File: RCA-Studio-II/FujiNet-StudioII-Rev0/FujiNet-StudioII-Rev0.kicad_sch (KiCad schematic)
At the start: 0 parts

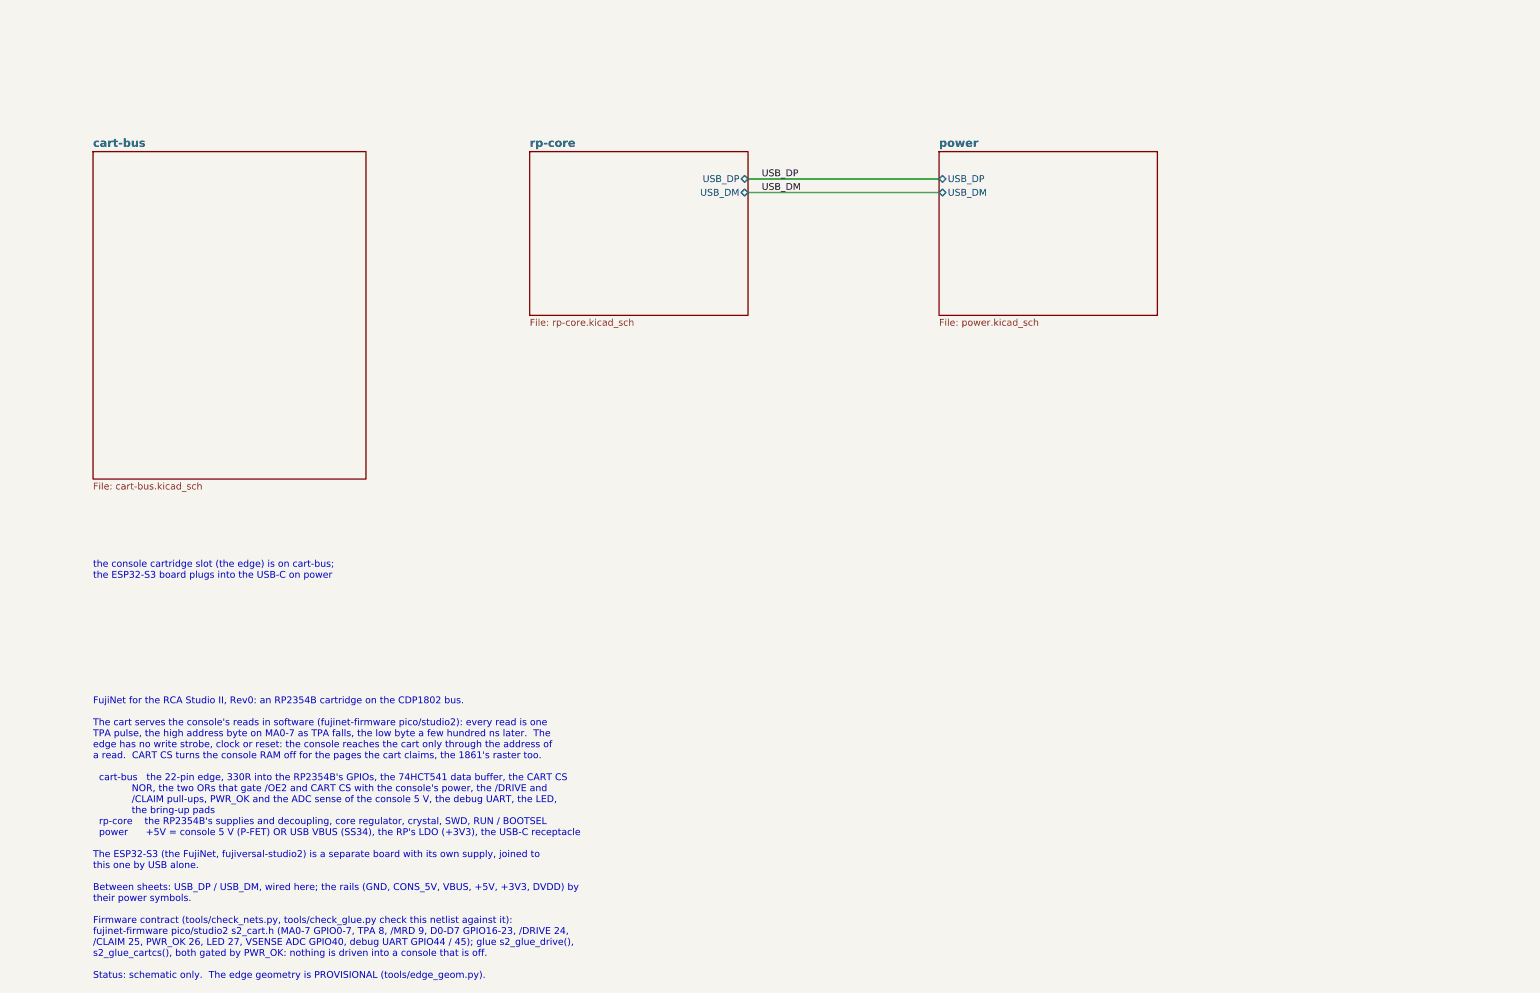
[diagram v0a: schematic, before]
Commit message: Studio II Rev0: ESP32-S3 on the cart, 4-layer board, JLCPCB package
The schematic is redone with the FujiNet's ESP32-S3 on the cartridge (it was
on a separate board), and the board is laid out, routed and audited for
JLCPCB assembly.

Schematic (5 sheets: cart-bus, rp-core, fujinet, usb, power):
- ESP32-S3-WROOM-1-N16R8 as the FujiNet and the RP2354B's USB host, with
  microSD, WS2812, EN RC and buttons (ported from FujiNet-ChannelF Rev0)
- USB-C -> USBLC6-2SC6 -> CP2102N with the UMH3N auto-program pair
- a TPS2116 power mux (USB first, the console's 5 V second) replaces the
  P-FET / SS34 OR, so the 74HCT glue stays at >= 4.72 V on either source
- AP63203 buck for the S3 side; RESET reaches both MCUs; the S3 drives the
  RP's RUN / BOOTSEL through 1k
- ERC 0, netlist parity 97 / 97, check_nets 364 / 0 failed / 1 warning
  (fujiversal-studio2.h lacks PIN_RP2040_RUN / _BOOTSEL), margins positive

Board: FliP's multicart outline from the insertion edge, 28 mm taller
(90.9 x 111.5 mm, printed shell), 22 hard-gold fingers on B.Cu, 4 layers,
every part on F.Cu; the S3 flush at the top edge with its antenna keep-out.
- KiCad DRC with schematic parity, all severities: 0 / 0 / 0, on the
  saved zone fills; layout_checks 65 / 65; check_fab 10 / 10
- LAYOUT=1 regenerates and re-routes it from scratch with every gate green

Fixes found by the audit, each now in the generator and gated:
- the gerbers plotted stale zone fills: 427 GND vias sat inside the In2
  power pours. tools/fill_zones.py refills after the last via, DRC runs
  on the saved fills, export uses --check-zones, and check_gerbers.py
  check 9 tests every plated hole against the plotted inner layers
- a 20 mm D+ loop at the flow-through USBLC6: twin pins now joined under
  the body, its 100 nF moved to the VBUS pin as ST draws it
- the USB-C 1.35 mm inside the edge: moved to HRO's layout (face 0.46 mm
  past the edge), USB-C and microSD 3D models fixed (FujiNet-NES 63ccf57)
- the antenna keep-out added as board ru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
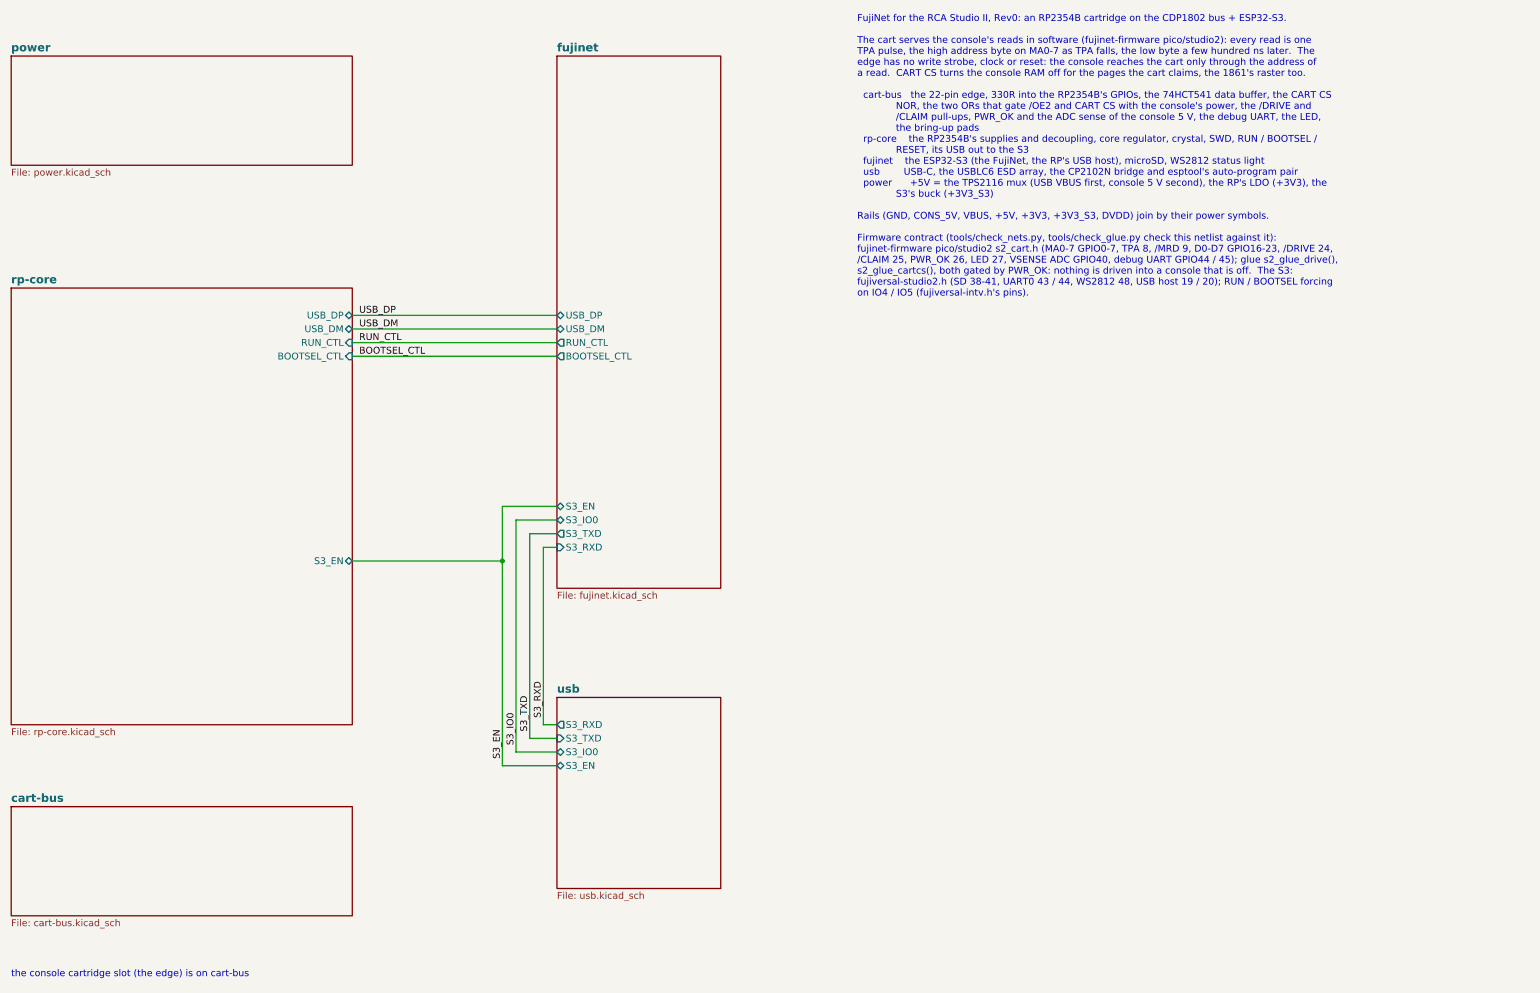
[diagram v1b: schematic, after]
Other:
- added sheet fujinet (fujinet.kicad_sch)
- added sheet usb (usb.kicad_sch)
- sheet power ports: added none; removed USB_DM, USB_DP
- sheet rp-core ports: added BOOTSEL_CTL, RUN_CTL, S3_EN; removed none
- note added: "FujiNet for the RCA Studio II, Rev0: an RP2354B cartridge on the CDP1802 bus + ESP32-S3. The cart serves the console's reads in software (fujinet-firmware pico/studio2): every read is one TPA pulse, the high address byte on MA0-7 as TPA falls, the low byte a few hundred ns later. The edge has no write strobe, clock or reset: the console reaches the cart only through the address of a read. CART CS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"
- note added: "the console cartridge slot (the edge) is on cart-bus"
- note removed: "FujiNet for the RCA Studio II, Rev0: an RP2354B cartridge on the CDP1802 bus. The cart serves the console's reads in software (fujinet-firmware pico/studio2): every read is one TPA pulse, the high address byte on MA0-7 as TPA falls, the low byte a few hundred ns later. The edge has no write strobe, clock or reset: the console reaches the cart only through the address of a read. CART CS turns the 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"
- note removed: "the console cartridge slot (the edge) is on cart-bus; the ESP32-S3 board plugs into the USB-C on power"
